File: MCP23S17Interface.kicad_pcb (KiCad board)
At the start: 2 copper layers, 55.8 x 45.4 mm, 6 parts, among them J1 Conn_01x09, J2 Conn_01x16, SW1 Address Selection, U1 MCP23S17_SP

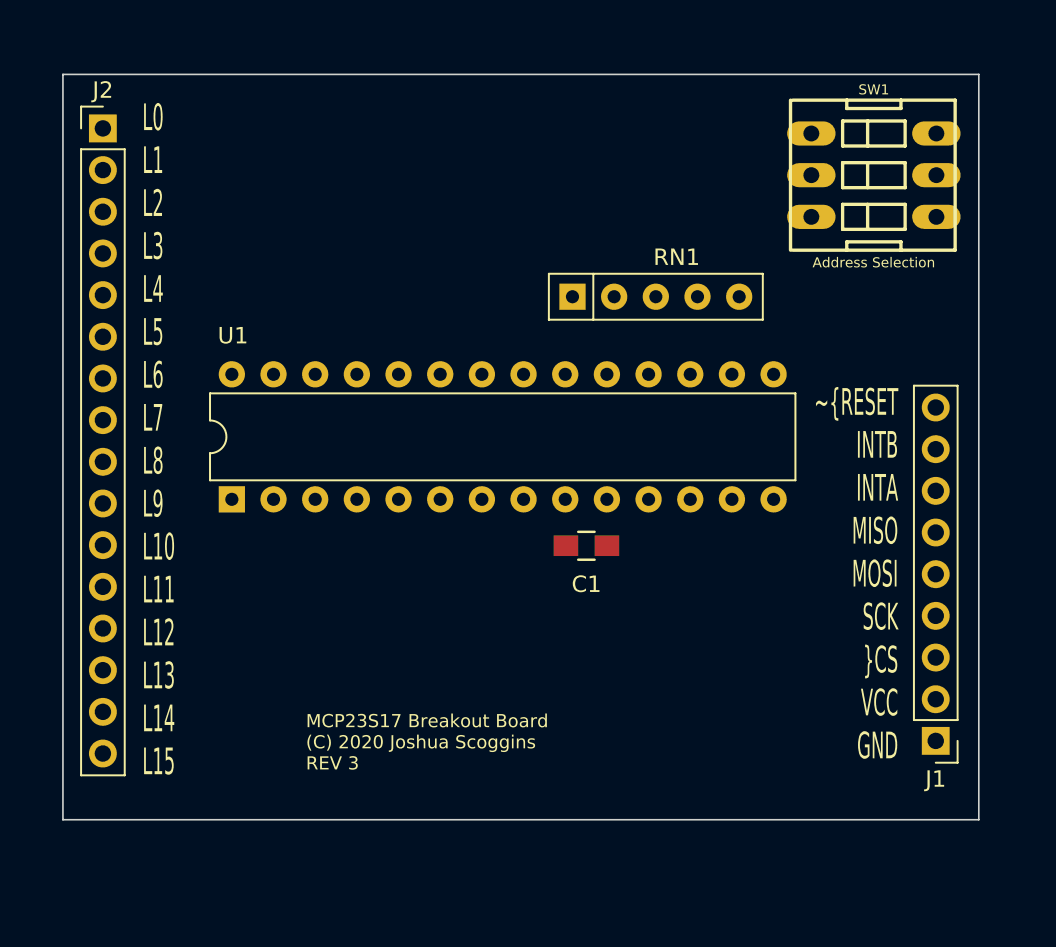
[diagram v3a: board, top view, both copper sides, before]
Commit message: Moved the connector up
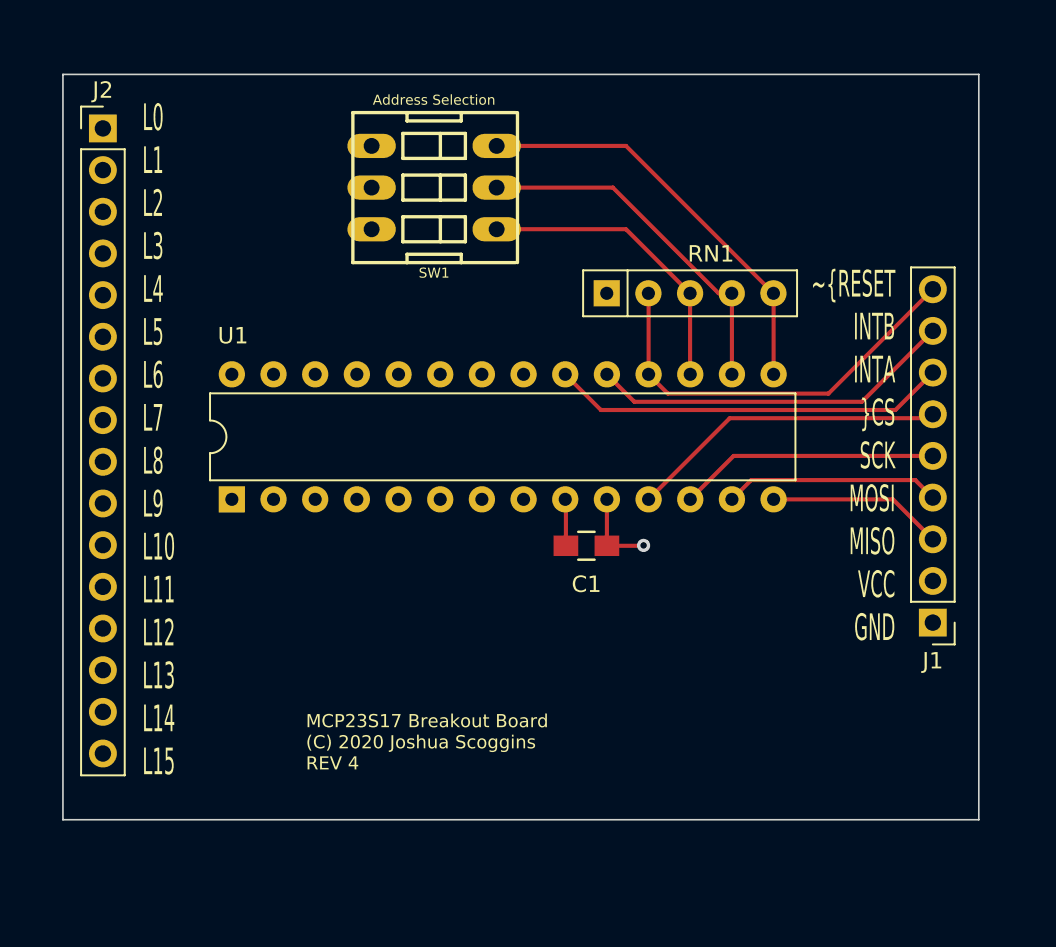
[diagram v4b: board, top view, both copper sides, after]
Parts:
- moved SW1 29.3 mm to (114.6, 29.2), turned to 90 degrees
- moved J1 7.21 mm to (145.0, 62.1)
- moved RN1 2.10 mm to (125.1, 42.0)
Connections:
- J1 pad 3: /~CS -> /MISO
- J1 pad 4: /SCK -> /MOSI
- J1 pad 5: /MOSI -> /SCK
- J1 pad 6: /MISO -> /~CS
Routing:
- net /A0: track 0.00 -> 25.5 mm
- net /~RESET: track 0.00 -> 25.4 mm
- net /INTA: track 0.00 -> 24.3 mm
- net /INTB: track 0.00 -> 22.3 mm
- net /A1: track 0.00 -> 21.9 mm
- net /~CS: track 0.00 -> 19.5 mm
- net /A2: track 0.00 -> 18.3 mm
- net /SCK: track 0.00 -> 15.9 mm
- net /MOSI: track 0.00 -> 13.2 mm
- net /MISO: track 0.00 -> 10.7 mm
- net GND: track 0.00 -> 5.07 mm, vias 0 -> 1
- net VCC: track 0.00 -> 2.85 mm
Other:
- board text added: "MCP23S17 Breakout Board (C) 2020 Joshua Scoggins REV 4"
- board text added: "~RESET INTB INTA ~CS SCK MOSI MISO VCC GND"
- board text removed: "MCP23S17 Breakout Board (C) 2020 Joshua Scoggins REV 3"
- board text removed: "~RESET INTB INTA MISO MOSI SCK ~CS VCC GND"
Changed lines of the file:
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@@
     (thickness 1.6002)
     (drawings 7)
-    (tracks 0)
+    (tracks 41)
     (zones 0)
     (modules 6)
@@
   )
   (module Switches:DIPSWITCH-03 (layer Front)
-    (at 141.4272 41.13784 270)
+    (at 114.62512 29.19476 90)
     (descr "3-POSITION DIP SWITCH - PTH, 0.1\"-PITCH")
     (tags "3-POSITION DIP SWITCH - PTH, 0.1\"-PITCH")
@@
       (effects (font (size 1.524 1.524) (thickness 0.1524)))
     )
-    (pad 6 thru_hole oval (at -8.89 -3.81 90) (size 1.47574 2.95402) (drill 0.96774) (layers *.Cu *.Mask)
+    (pad 6 thru_hole oval (at -8.89 -3.81 270) (size 1.47574 2.95402) (drill 0.96774) (layers *.Cu *.Mask)
       (net 1 GND) (solder_mask_margin 0.1016))
-    (pad 5 thru_hole oval (at -6.35 -3.81 90) (size 1.47574 2.95402) (drill 0.96774) (layers *.Cu *.Mask)
+    (pad 5 thru_hole oval (at -6.35 -3.81 270) (size 1.47574 2.95402) (drill 0.96774) (layers *.Cu *.Mask)
       (net 1 GND) (solder_mask_margin 0.1016))
-    (pad 4 thru_hole oval (at -3.81 -3.81 90) (size 1.47574 2.95402) (drill 0.96774) (layers *.Cu *.Mask)
+    (pad 4 thru_hole oval (at -3.81 -3.81 270) (size 1.47574 2.95402) (drill 0.96774) (layers *.Cu *.Mask)
       (net 1 GND) (solder_mask_margin 0.1016))
-    (pad 3 thru_hole oval (at -3.81 3.81 90) (size 1.47574 2.95402) (drill 0.96774) (layers *.Cu *.Mask)
+    (pad 3 thru_hole oval (at -3.81 3.81 270) (size 1.47574 2.95402) (drill 0.96774) (layers *.Cu *.Mask)
       (net 5 /A0) (solder_mask_margin 0.1016))
-    (pad 2 thru_hole oval (at -6.35 3.81 90) (size 1.47574 2.95402) (drill 0.96774) (layers *.Cu *.Mask)
+    (pad 2 thru_hole oval (at -6.35 3.81 270) (size 1.47574 2.95402) (drill 0.96774) (layers *.Cu *.Mask)
       (net 4 /A1) (solder_mask_margin 0.1016))
-    (pad 1 thru_hole oval (at -8.89 3.81 90) (size 1.47574 2.95402) (drill 0.96774) (layers *.Cu *.Mask)
+    (pad 1 thru_hole oval (at -8.89 3.81 270) (size 1.47574 2.95402) (drill 0.96774) (layers *.Cu *.Mask)
       (net 3 /A2) (solder_mask_margin 0.1016))
   )
   (module Resistor_THT:R_Array_SIP5 (layer Front)
-    (at 123.05792 42.19702)
+    (at 125.1458 41.98874)
     (descr "5-pin Resistor SIP pack")
     (tags R)
@@
   )
   (module Connector_PinHeader_2.54mm:PinHeader_1x09_P2.54mm_Vertical (layer Front)
-    (at 145.1991 69.26834 180)
+    (at 145.0213 62.05982 180)
     (descr "Through hole straight pin header, 1x09, 2.54mm pitch, single row")
     (tags "Through hole pin header THT 1x09 2.54mm single row")
@@
       (net 7 /INTA))
     (pad 6 thru_hole oval (at 0 12.7 180) (size 1.7 1.7) (drill 1) (layers *.Cu *.Mask)
+      (net 12 /~CS))
+    (pad 5 thru_hole oval (at 0 10.16 180) (size 1.7 1.7) (drill 1) (layers *.Cu *.Mask)
+      (net 11 /SCK))
+    (pad 4 thru_hole oval (at 0 7.62 180) (size 1.7 1.7) (drill 1) (layers *.Cu *.Mask)
+      (net 10 /MOSI))
+    (pad 3 thru_hole oval (at 0 5.08 180) (size 1.7 1.7) (drill 1) (layers *.Cu *.Mask)
       (net 9 /MISO))
-    (pad 5 thru_hole oval (at 0 10.16 180) (size 1.7 1.7) (drill 1) (layers *.Cu *.Mask)
-      (net 10 /MOSI))
-    (pad 4 thru_hole oval (at 0 7.62 180) (size 1.7 1.7) (drill 1) (layers *.Cu *.Mask)
-      (net 11 /SCK))
-    (pad 3 thru_hole oval (at 0 5.08 180) (size 1.7 1.7) (drill 1) (layers *.Cu *.Mask)
-      (net 12 /~CS))
     (pad 2 thru_hole oval (at 0 2.54 180) (size 1.7 1.7) (drill 1) (layers *.Cu *.Mask)
       (net 2 VCC))
@@
   (gr_line (start 92.00134 74.07402) (end 92.00134 28.64612) (layer Edge.Cuts) (width 0.1))
   (gr_line (start 147.82292 74.07402) (end 92.00134 74.07402) (layer Edge.Cuts) (width 0.1))
-  (gr_text "MCP23S17 Breakout Board\n(C) 2020 Joshua Scoggins\nREV 3" (at 106.807 69.350713) (layer F.SilkS)
+  (gr_text "MCP23S17 Breakout Board\n(C) 2020 Joshua Scoggins\nREV 4" (at 106.807 69.350713) (layer F.SilkS)
     (effects (font (size 0.8 0.8) (thickness 0.1)) (justify left))
   )
@@
     (effects (font (size 1.6256 0.8) (thickness 0.1)) (justify left))
   )
-  (gr_text "~RESET\nINTB\nINTA\nMISO\nMOSI\nSCK\n~CS\nVCC\nGND" (at 142.91564 59.10834) (layer F.SilkS)
+  (gr_text "~RESET\nINTB\nINTA\n~CS\nSCK\nMOSI\nMISO\nVCC\nGND" (at 142.73784 51.89982) (layer F.SilkS)
     (effects (font (size 1.6256 0.8) (thickness 0.1)) (justify right))
   )
+  (segment (start 125.15628 54.54682) (end 125.15596 54.5465) (width 0.25) (layer Front) (net 1))
+  (segment (start 125.15628 57.37606) (end 125.15628 54.54682) (width 0.25) (layer Front) (net 1))
+  (via (at 127.39116 57.3532) (size 0.8) (drill 0.4) (layers Front Back) (net 1))
+  (segment (start 125.15628 57.37606) (end 127.3683 57.37606) (width 0.25) (layer Front) (net 1))
+  (segment (start 127.3683 57.37606) (end 127.39116 57.3532) (width 0.25) (layer Front) (net 1))
+  (segment (start 122.65628 54.58682) (end 122.61596 54.5465) (width 0.25) (layer Front) (net 2))
+  (segment (start 122.65628 57.37606) (end 122.65628 54.58682) (width 0.25) (layer Front) (net 2))
+  (segment (start 126.32182 38.08476) (end 130.2258 41.98874) (width 0.25) (layer Front) (net 3))
+  (segment (start 118.43512 38.08476) (end 126.32182 38.08476) (width 0.25) (layer Front) (net 3))
+  (segment (start 130.2258 46.91634) (end 130.23596 46.9265) (width 0.25) (layer Front) (net 3))
+  (segment (start 130.2258 41.98874) (end 130.2258 46.91634) (width 0.25) (layer Front) (net 3))
+  (segment (start 131.964802 41.98874) (end 132.7658 41.98874) (width 0.25) (layer Front) (net 4))
+  (segment (start 125.520822 35.54476) (end 131.964802 41.98874) (width 0.25) (layer Front) (net 4))
+  (segment (start 118.43512 35.54476) (end 125.520822 35.54476) (width 0.25) (layer Front) (net 4))
+  (segment (start 132.77596 41.9989) (end 132.7658 41.98874) (width 0.25) (layer Front) (net 4))
+  (segment (start 132.77596 46.9265) (end 132.77596 41.9989) (width 0.25) (layer Front) (net 4))
+  (segment (start 135.31596 41.9989) (end 135.3058 41.98874) (width 0.25) (layer Front) (net 5))
+  (segment (start 135.31596 46.9265) (end 135.31596 41.9989) (width 0.25) (layer Front) (net 5))
+  (segment (start 126.32182 33.00476) (end 135.3058 41.98874) (width 0.25) (layer Front) (net 5))
+  (segment (start 118.43512 33.00476) (end 126.32182 33.00476) (width 0.25) (layer Front) (net 5))
+  (segment (start 126.830972 48.601512) (end 125.15596 46.9265) (width 0.25) (layer Front) (net 6))
+  (segment (start 140.699608 48.601512) (end 126.830972 48.601512) (width 0.25) (layer Front) (net 6))
+  (segment (start 145.0213 44.27982) (end 140.699608 48.601512) (width 0.25) (layer Front) (net 6))
+  (segment (start 142.739598 49.101522) (end 145.0213 46.81982) (width 0.25) (layer Front) (net 7))
+  (segment (start 124.790982 49.101522) (end 142.739598 49.101522) (width 0.25) (layer Front) (net 7))
+  (segment (start 122.61596 46.9265) (end 124.790982 49.101522) (width 0.25) (layer Front) (net 7))
+  (segment (start 127.69596 41.9989) (end 127.6858 41.98874) (width 0.25) (layer Front) (net 8))
+  (segment (start 127.69596 46.9265) (end 127.69596 41.9989) (width 0.25) (layer Front) (net 8))
+  (segment (start 128.870961 48.101501) (end 127.69596 46.9265) (width 0.25) (layer Front) (net 8))
+  (segment (start 138.659619 48.101501) (end 128.870961 48.101501) (width 0.25) (layer Front) (net 8))
+  (segment (start 145.0213 41.73982) (end 138.659619 48.101501) (width 0.25) (layer Front) (net 8))
+  (segment (start 142.58798 54.5465) (end 145.0213 56.97982) (width 0.25) (layer Front) (net 9))
+  (segment (start 135.31596 54.5465) (end 142.58798 54.5465) (width 0.25) (layer Front) (net 9))
+  (segment (start 143.952979 53.371499) (end 145.0213 54.43982) (width 0.25) (layer Front) (net 10))
+  (segment (start 133.950961 53.371499) (end 143.952979 53.371499) (width 0.25) (layer Front) (net 10))
+  (segment (start 132.77596 54.5465) (end 133.950961 53.371499) (width 0.25) (layer Front) (net 10))
+  (segment (start 132.88264 51.89982) (end 145.0213 51.89982) (width 0.25) (layer Front) (net 11))
+  (segment (start 130.23596 54.5465) (end 132.88264 51.89982) (width 0.25) (layer Front) (net 11))
+  (segment (start 144.779589 49.601531) (end 145.0213 49.35982) (width 0.25) (layer Front) (net 12))
+  (segment (start 132.64093 49.601531) (end 144.779589 49.601531) (width 0.25) (layer Front) (net 12))
+  (segment (start 127.69596 54.5465) (end 132.64093 49.601531) (width 0.25) (layer Front) (net 12))
   (zone (net 0) (net_name "") (layers F&B.Cu) (hatch edge 0.508)
     (connect_pads (clearance 0.508))
